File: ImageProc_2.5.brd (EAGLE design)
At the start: 46.6 x 21.9 mm, 116 parts, among them IC1 XC61GC3002HR-G, IC10 AT45DB642D-CNU, IC2 MIC5335-SPYMT, IC3 MIC5335-JGYMT, IC4 DSPIC33FJ128MC706A, IC5 AT86RF233-ZU, IC6 LTC6088, IC7 DRV8833RTY, IC8 DRV8833RTY, IC9 MPU-6000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

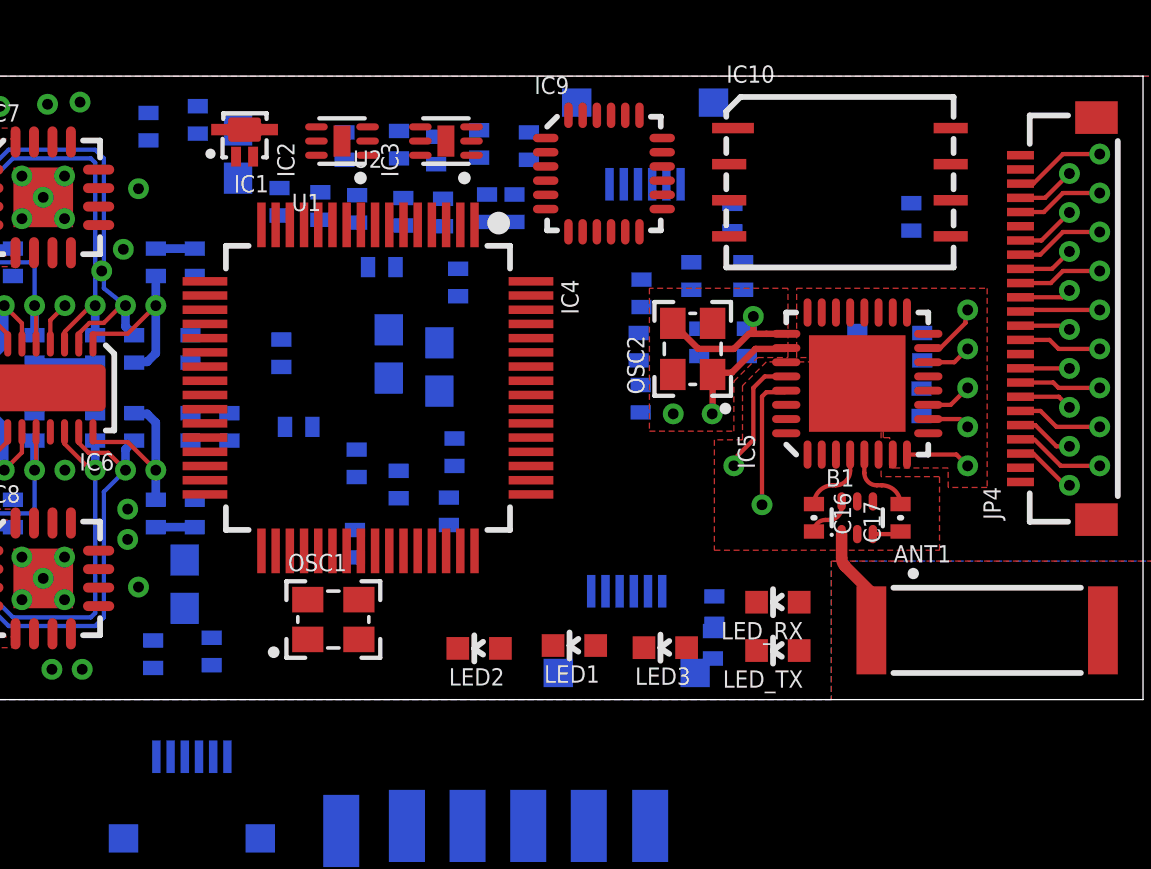
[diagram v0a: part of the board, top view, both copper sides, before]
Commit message: Added tPlace outlines to 0603s and 0402s
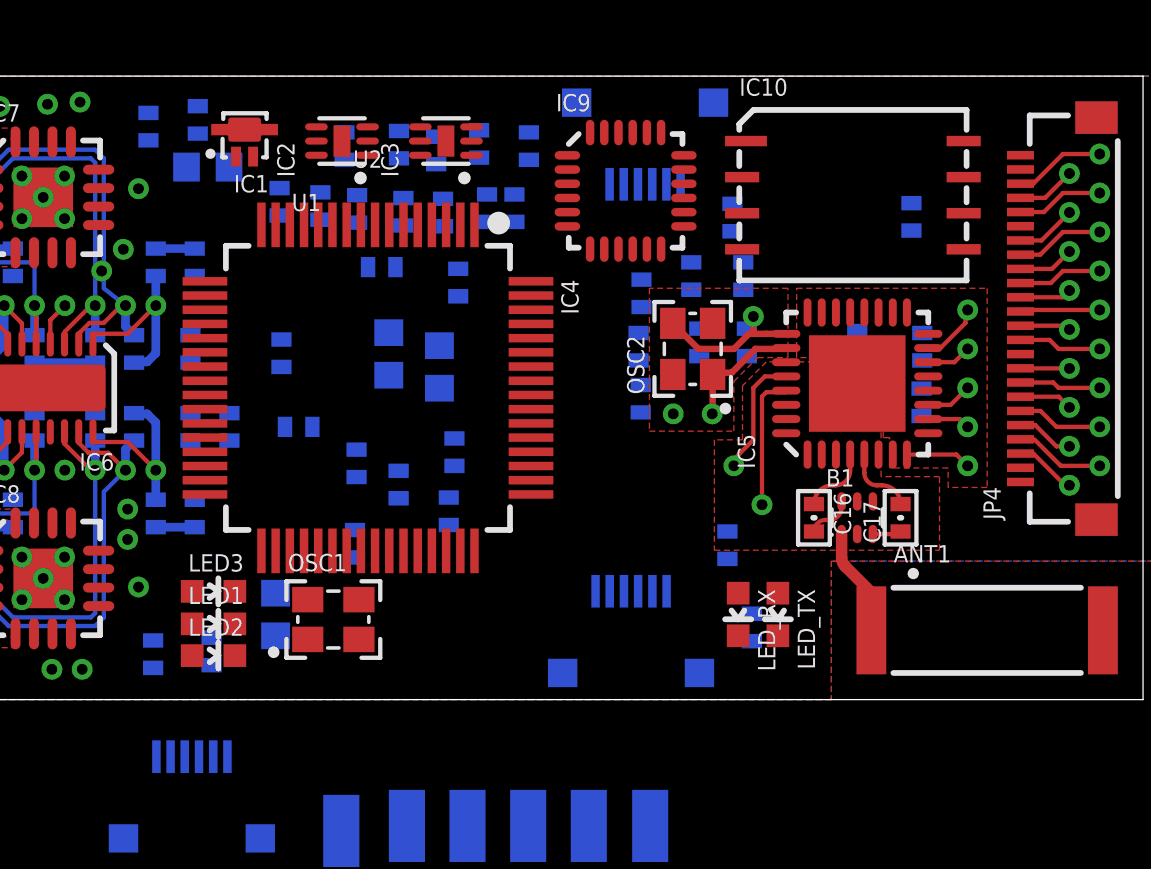
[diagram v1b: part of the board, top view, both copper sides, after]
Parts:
- moved LED3 16.0 mm to (13.9, 3.81), turned to 270 degrees
- moved LED1 12.7 mm to (13.9, 2.67), turned to 270 degrees
- moved LED2 9.35 mm to (13.9, 1.55), turned to 270 degrees
- moved C30 3.37 mm to (16.1, 3.00)
- moved R7 2.33 mm to (32.0, 5.44)
- moved R6 1.50 mm to (32.9, 2.54)
- moved LED_RX 1.46 mm to (32.4, 3.00), turned to 180 degrees
- moved LED_TX 1.27 mm to (33.8, 3.00), turned to 180 degrees
- moved C33 1.16 mm to (13.7, 18.7), turned to 0 degrees
- moved IC9 0.98 mm to (28.4, 17.9)
- moved IC10 0.65 mm to (36.4, 17.8)
- moved JP1 0.15 mm to (28.6, 2.09)

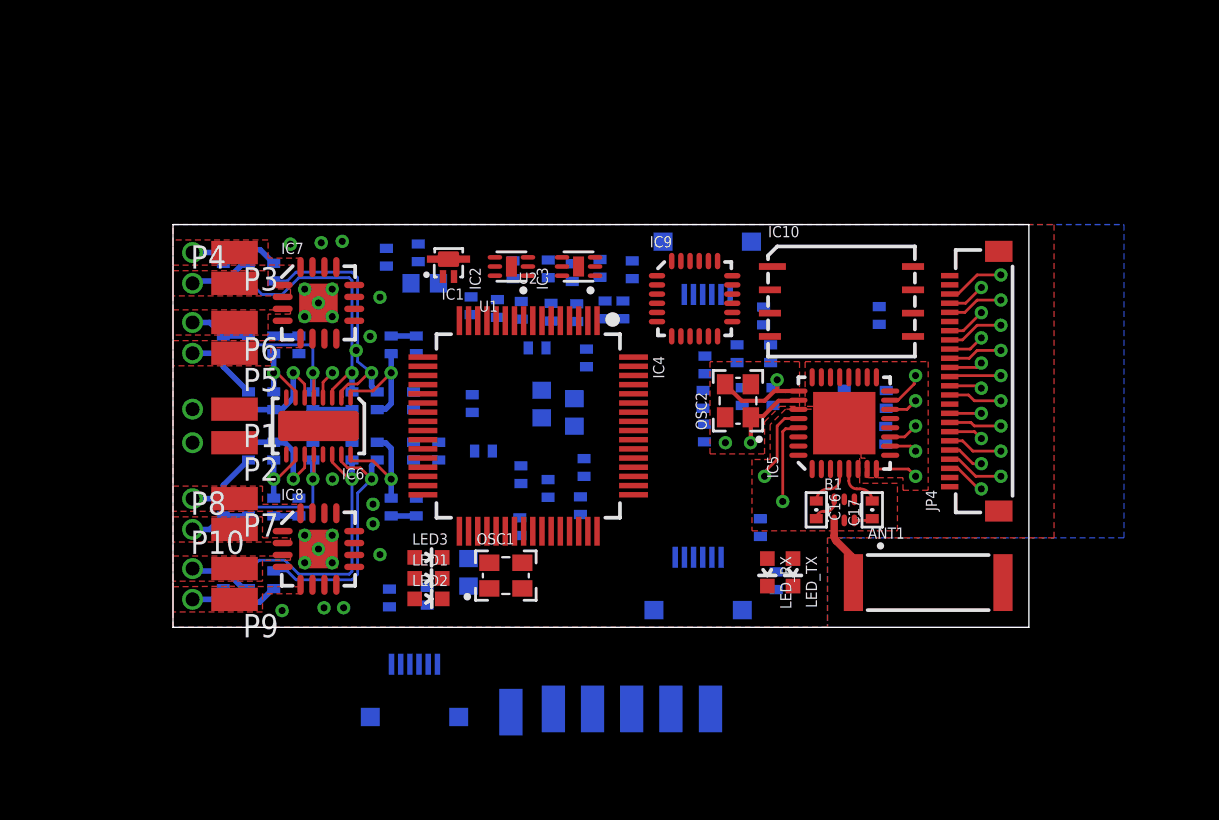
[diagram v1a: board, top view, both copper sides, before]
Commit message: Partial IMU/flash route. PIC, IMU, and flash locations locked. Passives for IMU/flash.
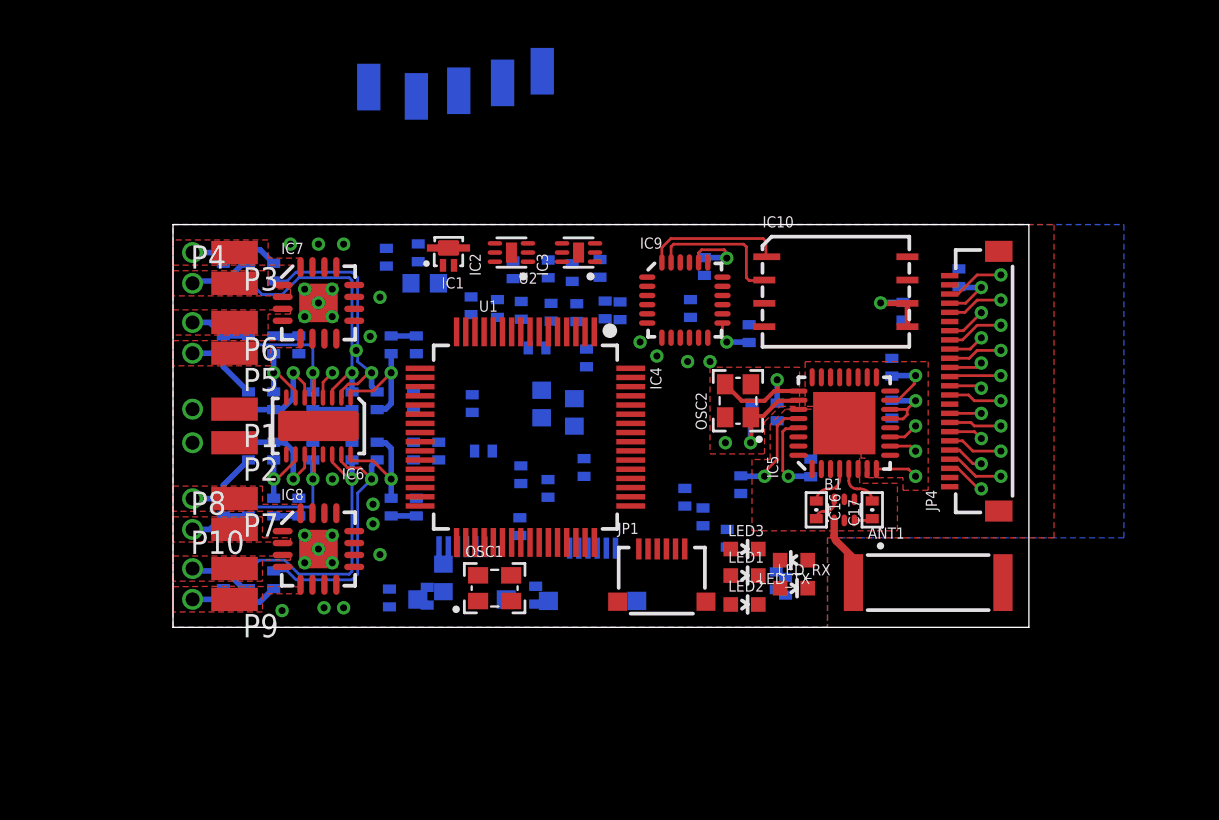
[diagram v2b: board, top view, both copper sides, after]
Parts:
- removed P15: EXT5, wirepad:SMD1,27-2,54
- moved P13 36.4 mm to (15.6, 29.2)
- moved P11 36.1 mm to (13.3, 28.9)
- moved P16 36.0 mm to (10.7, 29.4), turned to 180 degrees
- moved P12 35.1 mm to (20.1, 30.3)
- moved P14 34.3 mm to (18.0, 29.7)
- moved C36 18.4 mm to (42.8, 19.1), turned to 270 degrees
- moved JP3 18.4 mm to (22.9, 2.59), turned to 0 degrees
- moved LED3 17.2 mm to (31.1, 4.27)
- moved LED2 17.2 mm to (31.1, 1.24)
- moved LED1 17.2 mm to (31.1, 2.82)
- moved R27 9.53 mm to (30.2, 4.85)
- moved C21 7.35 mm to (30.9, 7.77), turned to 270 degrees
- moved JP2 6.91 mm to (15.7, 2.67)
- moved R26 6.40 mm to (28.9, 6.02)
- moved C9 5.45 mm to (19.8, 1.75)
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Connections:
- removed net EXT5: IC4.42, P15.1
- new net CAM_D5: IC4.53
- new net IMU_IRQ: IC4.42, IC9.12
- net N#3: no longer IC4.53
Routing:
- net 3.3V: track 8.07 -> 17.0 mm, vias 3 -> 5
- net SCK2: track 0.00 -> 7.81 mm
- net SDO2: track 0.00 -> 7.61 mm
- net N$29: track 0.00 -> 3.73 mm, vias 0 -> 1
- net N$1: track 1.58 -> 4.22 mm
- net N$9: track 4.44 -> 5.78 mm
- net N$8: track 5.20 -> 6.47 mm
- net 2.5V: track 3.90 -> 5.14 mm

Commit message: Motor section mostly complete. Board expanded. PIC passives mostly complete.
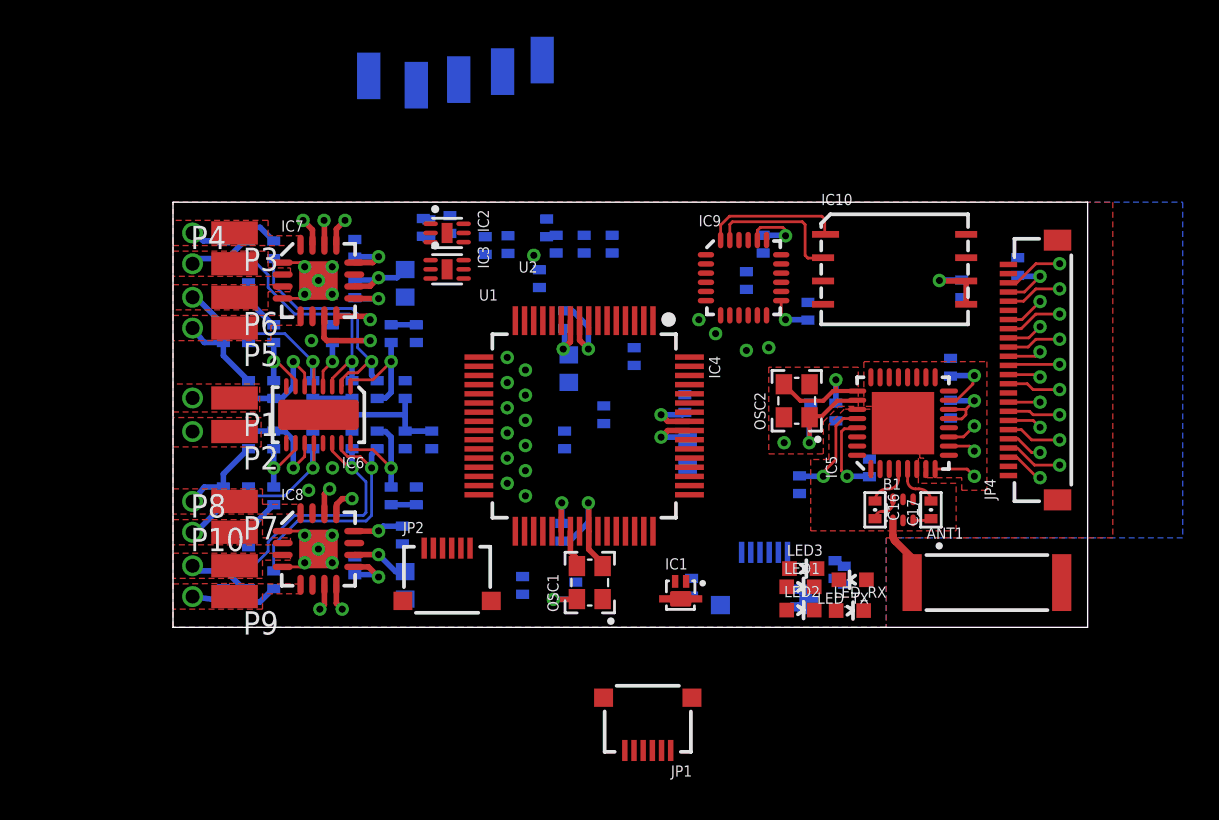
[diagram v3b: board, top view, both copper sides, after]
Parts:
- moved IC1 22.6 mm to (27.7, 1.75), turned to 0 degrees
- moved C33 16.5 mm to (12.6, 2.29), turned to 270 degrees
- moved C30 16.2 mm to (12.6, 18.7), turned to 270 degrees
- moved C11 11.5 mm to (21.3, 16.8)
- moved R2 11.3 mm to (13.9, 21.7), turned to 270 degrees
- moved R4 10.3 mm to (19.1, 2.29), turned to 90 degrees
- moved C13 9.59 mm to (21.2, 5.18)
- moved R5 9.50 mm to (28.3, 2.18), turned to 270 degrees
- moved JP3 9.38 mm to (32.2, 2.36)
- moved C29 9.10 mm to (8.69, 16.0)
- moved C6 8.52 mm to (15.1, 21.9)
- moved R28 8.20 mm to (34.0, 1.60)
- moved JP1 7.57 mm to (25.9, -4.98), turned to 180 degrees
- moved C5 7.53 mm to (20.9, 20.9)
- moved IC3 7.22 mm to (14.9, 19.5), turned to 270 degrees
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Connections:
- net 3.3V: now also R16.2
- net V_BATT: no longer R16.2
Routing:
- net GND: track 0.00 -> 16.6 mm, vias 13 -> 16
- net 3.3V: track 17.0 -> 29.2 mm, vias 5 -> 10
- net V_BATT: track 0.00 -> 9.41 mm, vias 1 -> 4
- net V_REF: track 5.69 -> 11.8 mm
- net 2.5V: track 5.14 -> 10.1 mm
- net MOTOR_B_IN1: track 0.00 -> 3.76 mm, vias 0 -> 1
- net N$28: track 0.00 -> 3.19 mm, vias 0 -> 1
- net N$19: track 0.00 -> 2.90 mm, vias 0 -> 1
- net N$18: track 0.00 -> 2.77 mm, vias 0 -> 1
- net N$20: track 0.00 -> 2.73 mm, vias 0 -> 1
- net N$2: track 0.00 -> 2.65 mm, vias 0 -> 1
- net 40MHZ: track 1.78 -> 3.82 mm
- net MOTOR_B_IN2: track 0.00 -> 1.92 mm, vias 0 -> 1
- net MOTOR_A_IN2: track 0.00 -> 1.77 mm, vias 0 -> 1
- net N$31: track 14.3 -> 12.7 mm
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- added copper zone on layer 1, net V_BATT
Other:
- board size 46.6 x 21.9 mm -> 49.8 x 23.2 mm

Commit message: PIC and radio vias added. Partial camera route.
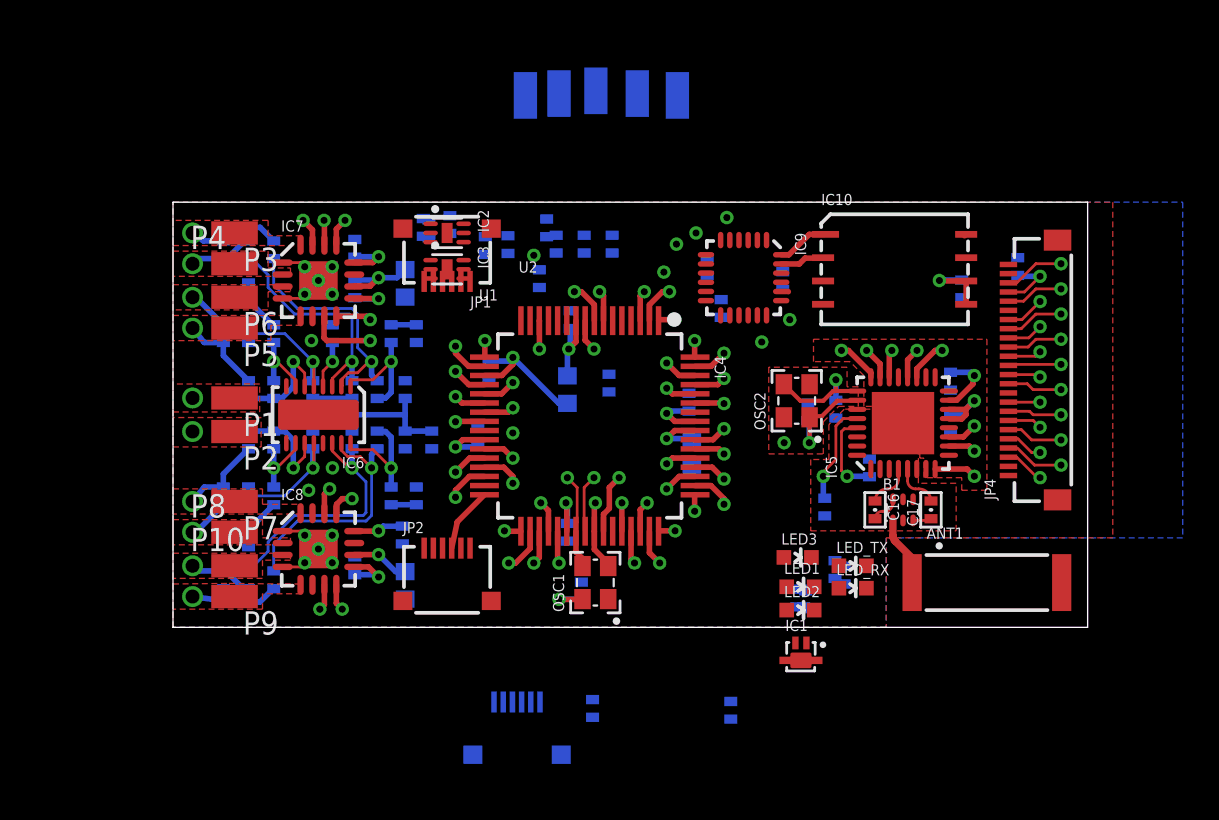
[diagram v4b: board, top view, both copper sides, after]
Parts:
- moved JP1 27.8 mm to (14.9, 20.6)
- moved JP3 15.8 mm to (18.7, -5.79)
- moved P14 9.61 mm to (27.5, 29.0)
- moved P16 8.60 mm to (19.2, 29.0)
- moved P11 7.79 mm to (21.0, 29.1)
- moved R4 7.71 mm to (22.9, -4.42), turned to 270 degrees
- moved P13 7.49 mm to (23.0, 29.2)
- moved IC1 7.36 mm to (34.2, -1.60)
- moved R5 7.04 mm to (30.4, -4.52)
- moved C10 6.71 mm to (17.2, 14.0)
- moved P12 5.49 mm to (25.3, 29.1)
- moved C12 4.73 mm to (16.6, 10.4)
- moved C40 4.73 mm to (29.9, 17.4)
- moved C39 2.27 mm to (29.1, 19.7)
- moved C38 2.25 mm to (33.2, 18.9), turned to 270 degrees
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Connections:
- removed net N#3: JP4.9
- net CAM_D5: now also JP4.9
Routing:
- net RADIO_SLP_TR: track 1.63 -> 34.2 mm
- net CAM_D0: track 3.02 -> 31.5 mm, vias 1 -> 2
- net CAM_D5: track 0.00 -> 27.3 mm, vias 0 -> 2
- net CAM_D3: track 2.03 -> 25.5 mm, vias 1 -> 2
- net CAM_D1: track 2.69 -> 25.2 mm, vias 1 -> 2
- net CAM_D4: track 1.88 -> 23.3 mm, vias 1 -> 2
- net CAM_D2: track 2.19 -> 22.2 mm, vias 1 -> 2
- net N$21: track 0.00 -> 7.56 mm, vias 0 -> 1
- net SCK2: track 7.81 -> 2.42 mm
- net SDO2: track 7.61 -> 2.88 mm
- net RADIO_IRQ: track 0.00 -> 4.16 mm, vias 0 -> 2
- net SDI1: track 0.00 -> 4.11 mm, vias 0 -> 2
- net SCK1: track 0.00 -> 4.11 mm, vias 0 -> 2
- net GND: track 16.6 -> 12.7 mm, vias 16 -> 17
- net N$29: track 3.73 -> 0.02 mm
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
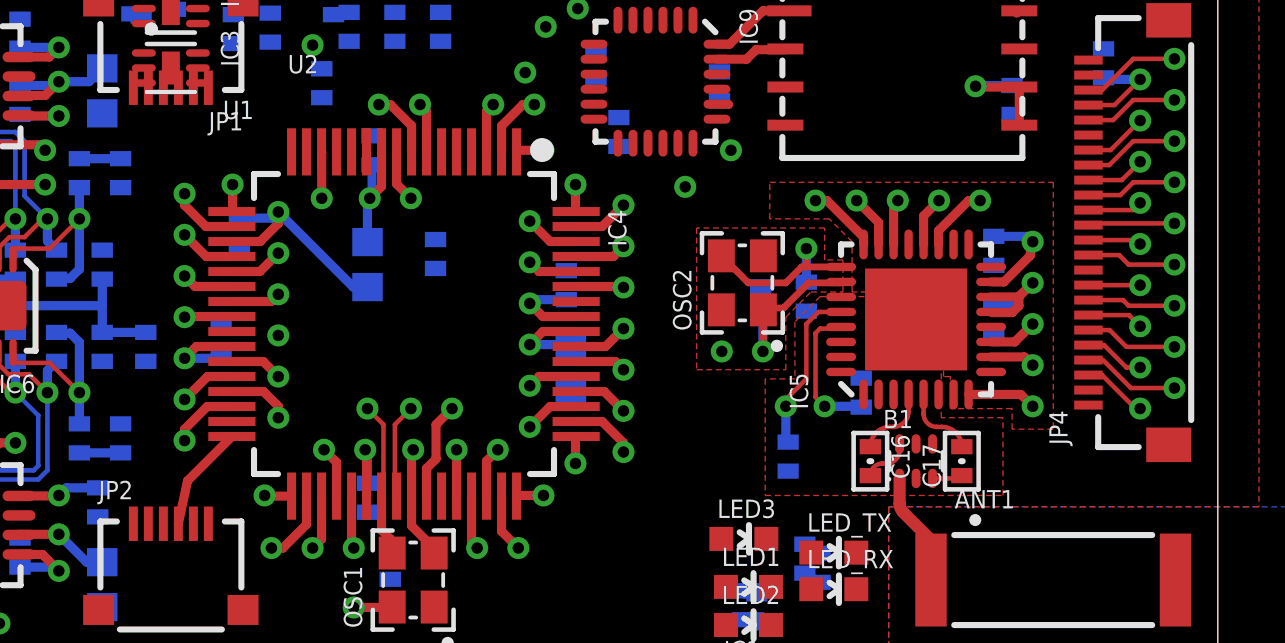
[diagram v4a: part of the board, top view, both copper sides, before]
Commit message: More camera connector routed. Vias on right side of PIC re-spaced.
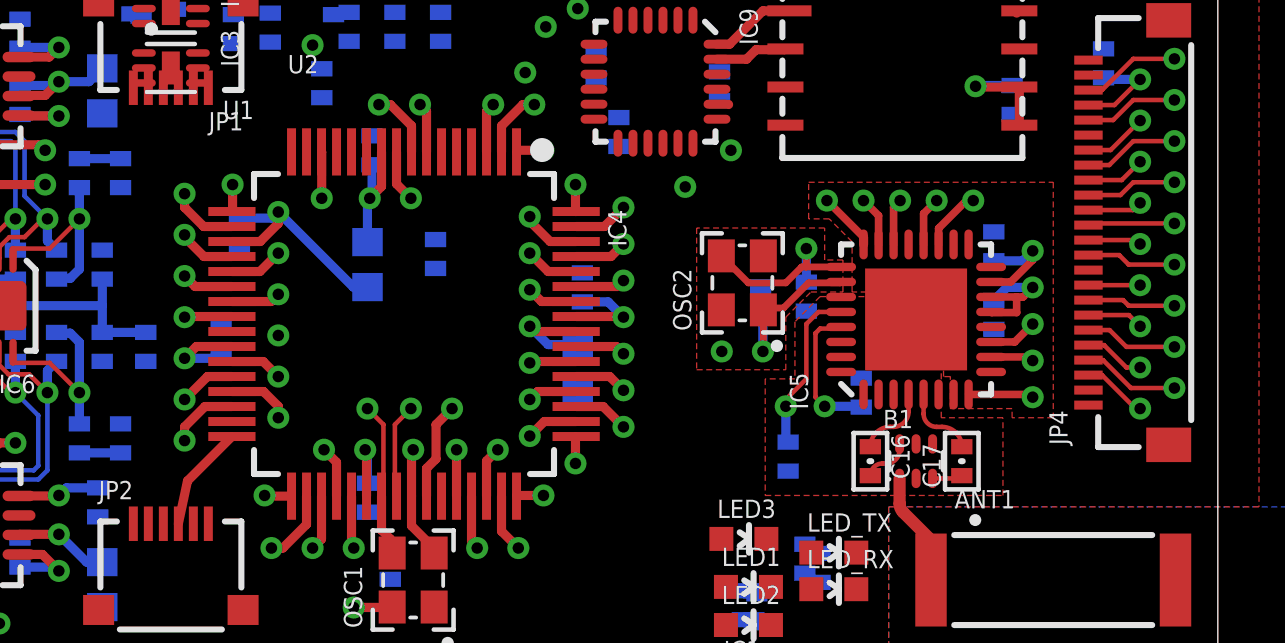
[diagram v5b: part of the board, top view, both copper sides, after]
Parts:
- moved C14 0.54 mm to (28.7, 12.2)
- moved C15 0.24 mm to (28.5, 9.45)
- moved C22 0.15 mm to (42.4, 11.3)
- moved C23 0.15 mm to (42.4, 13.6), turned to 90 degrees
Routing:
- net CAM_HREF: track 1.98 -> 26.9 mm, vias 2 -> 3
- net CAM_D7: track 4.71 -> 27.6 mm
- net CAM_PCLK: track 4.53 -> 24.1 mm
- net CAM_D5: track 27.3 -> 24.2 mm
- net CAM_D4: track 23.3 -> 26.4 mm
- net CAM_D3: track 25.5 -> 22.4 mm
- net CAM_D2: track 22.2 -> 25.1 mm
